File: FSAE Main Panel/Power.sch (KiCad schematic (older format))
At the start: 42 parts, among them Q301 IRLML6402TRPBF, U301 TPS53513, U302 LM2940IMP-5.0/NOPB, U303 LP5907MFX-3.3, U304 LP5907MFX-3.3, U305 LP5907MFX-3.3

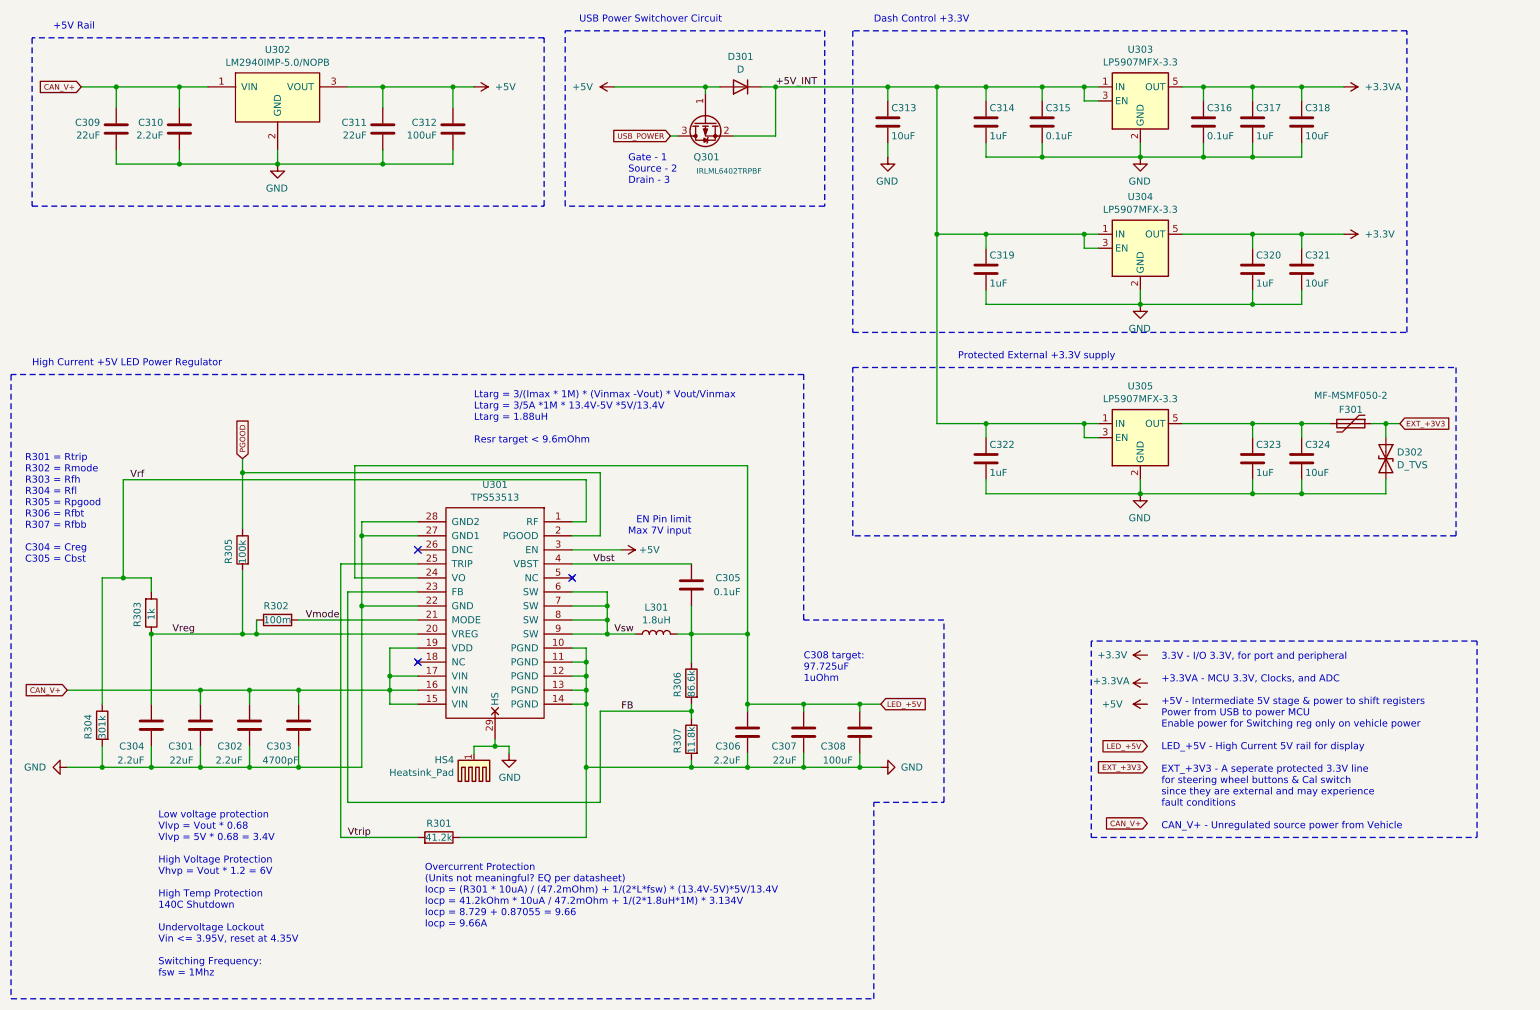
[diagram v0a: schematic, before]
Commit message: Changed Display Power Reg
Swapped costly complex 5V Rail reg for smaller lower efficiency TPS564201
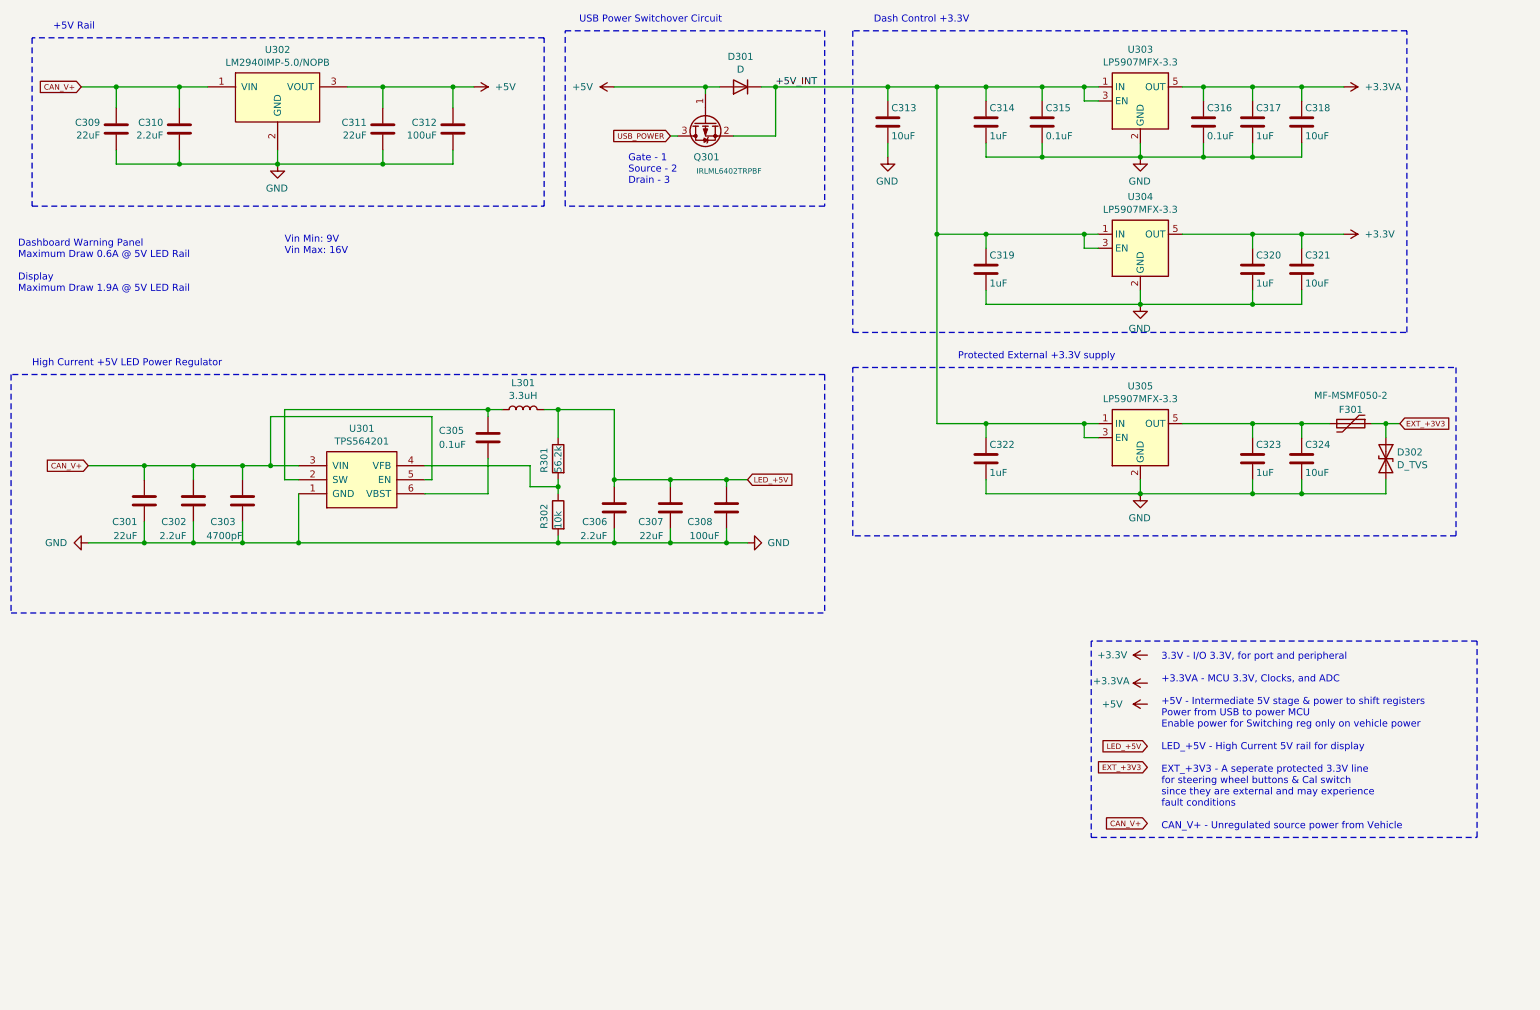
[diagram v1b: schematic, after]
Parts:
- removed C304: 2.2uF, Capacitors_SMD:C_1206, symbol Device:C
- removed HS4: Heatsink_Pad, symbol Mechanical:Heatsink_Pad
- removed R301: 41.2k, Resistors_SMD:R_0603, symbol Device:R
- removed R302: 100m, Resistors_SMD:R_0603, symbol Device:R
- removed R303: 1k, Resistors_SMD:R_0603, symbol Device:R
- removed R304: 301k, Resistors_SMD:R_0603, symbol Device:R
- removed R305: 100k, Resistors_SMD:R_0603, symbol Device:R
- removed U301: TPS53513, Texas_Additions:VQFN-CLIP-28-4.5x3.5mm, symbol TI_Additions:TPS53513
- added U301: TPS564201, TO_SOT_Packages_SMD:SOT-23-6, symbol FSAE2020:TPS564201
- L301: value 1.8uH -> 3.3uH; footprint FSAE2020:SRP1238A -> Inductors_SMD:L_Bourns-SRU8043; Description FIXED IND 1.8UH 17A 7 MOHM SMD -> FIXED IND 3.3UH 6.5A 11 MOHM SMD; Digikey P/N SRP1238A-1R8MCT-ND -> SRR1050A-3R3YCT-ND; Part Number SRP1238A-1R8M -> SRR1050A-3R3Y
- R301: renamed from R306; value 86.6k -> 56.2k; Description RES 86.6K OHM 1% 1/10W 0603 -> RES 56.2K OHM 1% 1/10W 0603; Digikey P/N RMCF0603FT86K6CT-ND -> RMCF0603FT56K2CT-ND; Part Number RMCF0603FT86K6 -> RMCF0603FT56K2
- R302: renamed from R307; value 11.8k -> 10k; Description RES 11.8K OHM 1% 1/10W 0603 -> RES 10K OHM 5% 1/10W 0603; Digikey P/N RMCF0603FT11K8CT-ND -> RMCF0603JT10K0CT-ND; Part Number RMCF0603FT11K8 -> RMCF0603JT10K0
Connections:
- net Vsw is gone; now on an unnamed net: L301.2
- net CAN_V+: now also U301.3 (VIN), U301.5 (EN)
- net GND: now also U301.1 (GND)
- net LED_+5V: no longer C305.2
- net FB: no longer names the net of R301.2, R302.1
- net FB: now also U301.4 (VFB)
- net Vbst: no longer names the net of C305.1
- net Vbst: now also U301.2 (SW)
- new net: C305.2, U301.6 (VBST)
- no-connect marks 3 -> 0
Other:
- note added: "Dashboard Warning Panel\nMaximum Draw 0.6A @ 5V LED Rail\n\nDisplay\nMaximum Draw 1.9A @ 5V LED Rail\n\n"
- note added: "Vin Min: 9V\nVin Max: 16V"
- note removed: "C308 target:\n97.725uF\n1uOhm"
- note removed: "EN Pin limit \nMax 7V input"
- note removed: "Low voltage protection\nVlvp = Vout * 0.68\nVlvp = 5V * 0.68 = 3.4V\n\nHigh Voltage Protection\nVhvp = Vout * 1.2 = 6V\n\nHigh Temp Protection\n140C Shutdown\n\nUndervoltage Lockout\nVin <= 3.95V, reset at 4.35V\n\nSwitching Frequency:\nfsw = 1Mhz"
- note removed: "Ltarg = 3/(Imax * 1M) * (Vinmax -Vout) * Vout/Vinmax\nLtarg = 3/5A *1M * 13.4V-5V *5V/13.4V\nLtarg = 1.88uH\n\nResr target < 9.6mOhm"
- note removed: "Overcurrent Protection\n(Units not meaningful? EQ per datasheet)\nIocp = (R301 * 10uA) / (47.2mOhm) + 1/(2*L*fsw) * (13.4V-5V)*5V/13.4V\nIocp = 41.2kOhm * 10uA / 47.2mOhm + 1/(2*1.8uH*1M) * 3.134V\nIocp = 8.729 + 0.87055 = 9.66\nIocp = 9.66A"
- note removed: "R301 = Rtrip\nR302 = Rmode\nR303 = Rfh\nR304 = Rfl\nR305 = Rpgood\nR306 = Rfbt\nR307 = Rfbb\n\nC304 = Creg\nC305 = Cbst\n"
- moved on the sheet: C301, C302, C303, C306, C307, C308, L301, R301, R302

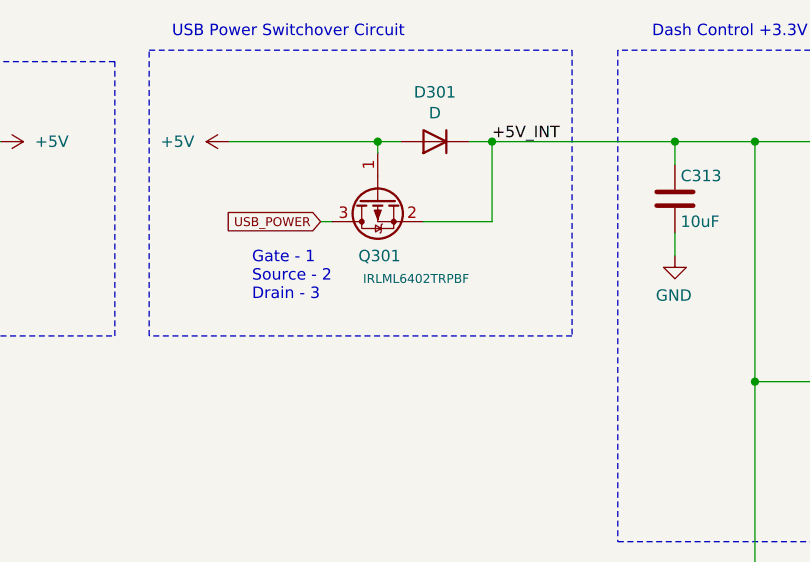
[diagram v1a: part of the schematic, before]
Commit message: Four Layer Shrink
Shifted edge connectors and associated components up to reduce board width for clearance issues.
Changed to four layer board for huge improvement on routing power and ground planes
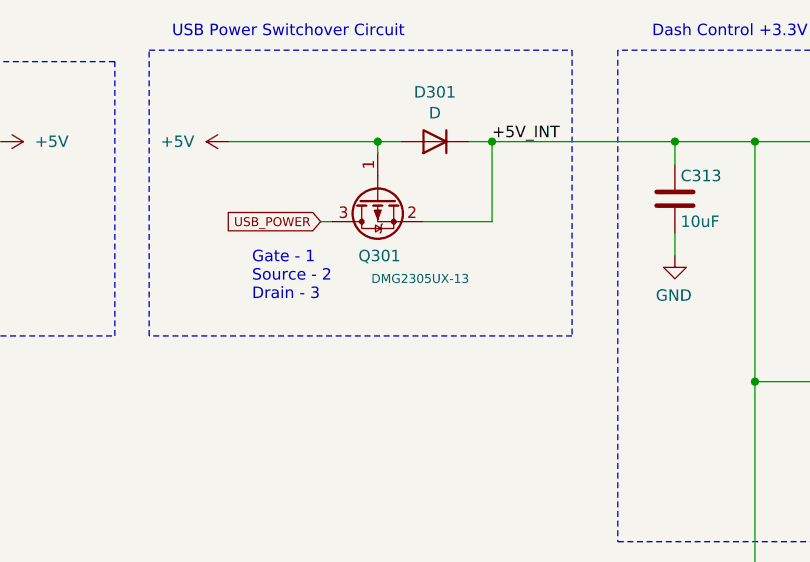
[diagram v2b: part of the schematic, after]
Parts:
- Q301: value IRLML6402TRPBF -> DMG2305UX-13; Digikey P/N IRLML6402PBFCT-ND -> DMG2305UX-13DICT-ND; Manufacturer Infineon -> Diodes Inc; Part Number IRLML6402TRPBF -> DMG2305UX-13
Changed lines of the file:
@@
 P 5650 1400
 F 0 "Q301" V 5900 1300 50  0000 L CNN
-F 1 "IRLML6402TRPBF" V 6000 1000 39  0000 L CNN
+F 1 "DMG2305UX-13" V 6000 1000 39  0000 L CNN
 F 2 "TO_SOT_Packages_SMD:SOT-23" H 5850 1500 50  0001 C CNN
-F 3 "https://www.infineon.com/dgdl/irlml6402pbf.pdf?fileId=5546d462533600a401535668d5c2263c" H 5650 1400 50  0001 C CNN
+F 3 "https://www.diodes.com/assets/Datasheets/DMG2305UX.pdf" H 5650 1400 50  0001 C CNN
 F 4 "MOSFET P-CH 20V 3.7A SOT-23" H 5650 1400 50  0001 C CNN "Description"
-F 5 "Infineon" H -350 -3700 50  0001 C CNN "Manufacturer"
-F 6 "IRLML6402TRPBF" H -350 -3700 50  0001 C CNN "Part Number"
-F 7 "IRLML6402PBFCT-ND" H 5650 1400 50  0001 C CNN "Digikey P/N"
+F 5 "Diodes Inc" H -350 -3700 50  0001 C CNN "Manufacturer"
+F 6 "DMG2305UX-13" H -350 -3700 50  0001 C CNN "Part Number"
+F 7 "DMG2305UX-13DICT-ND" H 5650 1400 50  0001 C CNN "Digikey P/N"
 	1    5650 1400
 	0    -1   1    0

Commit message: Hierarchical Sheets
Changed to Hierarchical Sheets structure and redid a few little details.
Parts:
- D302: Description TVS DIODE 5.5V 14V 2X1SON -> 11.5V Clamp 90A (8/20µs) Ipp Tvs Diode Surface Mount U-DFN1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; Digikey P/N 296-30406-1-ND -> D5V0H1U2LP1610-7DICT-ND; Manufacturer TI -> Diodes Inc; Part Number TPD1E10B06DPYR -> D5V0H1U2LP1610-7
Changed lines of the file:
@@
 F 1 "D_TVS" V 10545 3879 50  0000 L CNN
 F 2 "Resistors_SMD:R_0603" H 10500 3800 50  0001 C CNN
-F 3 "https://www.ti.com/lit/ds/symlink/tpd1e10b06.pdf" H 10500 3800 50  0001 C CNN
-F 4 "TVS DIODE 5.5V 14V 2X1SON" H 10500 3800 50  0001 C CNN "Description"
-F 5 "296-30406-1-ND" H 10500 3800 50  0001 C CNN "Digikey P/N"
-F 6 "TI" H 10500 3800 50  0001 C CNN "Manufacturer"
-F 7 "TPD1E10B06DPYR" H 10500 3800 50  0001 C CNN "Part Number"
+F 3 "https://www.diodes.com/assets/Datasheets/D5V0H1U2LP1610.pdf" H 10500 3800 50  0001 C CNN
+F 4 "11.5V Clamp 90A (8/20µs) Ipp Tvs Diode Surface Mount U-DFN1610-2 (Type B)" H 10500 3800 50  0001 C CNN "Description"
+F 5 "D5V0H1U2LP1610-7DICT-ND" H 10500 3800 50  0001 C CNN "Digikey P/N"
+F 6 "Diodes Inc" H 10500 3800 50  0001 C CNN "Manufacturer"
+F 7 "D5V0H1U2LP1610-7" H 10500 3800 50  0001 C CNN "Part Number"
 	1    10500 3800
 	0    1    1    0
